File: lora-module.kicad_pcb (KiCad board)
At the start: 4 copper layers, 27.3 x 24.5 mm, 37 parts, among them P1 CONN_01X07, P2 CONN_01X07, Q1 32MHz, U2 SX1276, U5 PE4259

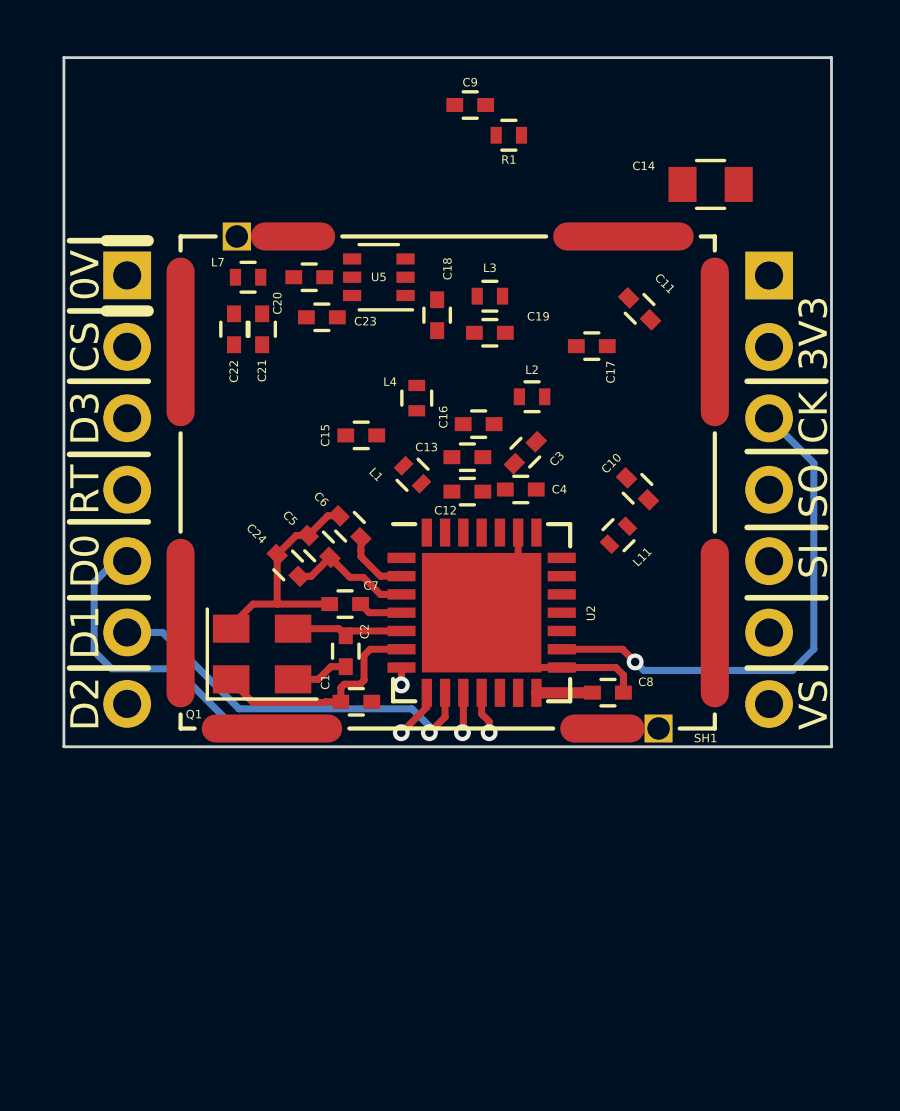
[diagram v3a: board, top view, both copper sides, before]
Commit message: added poligones for all layers
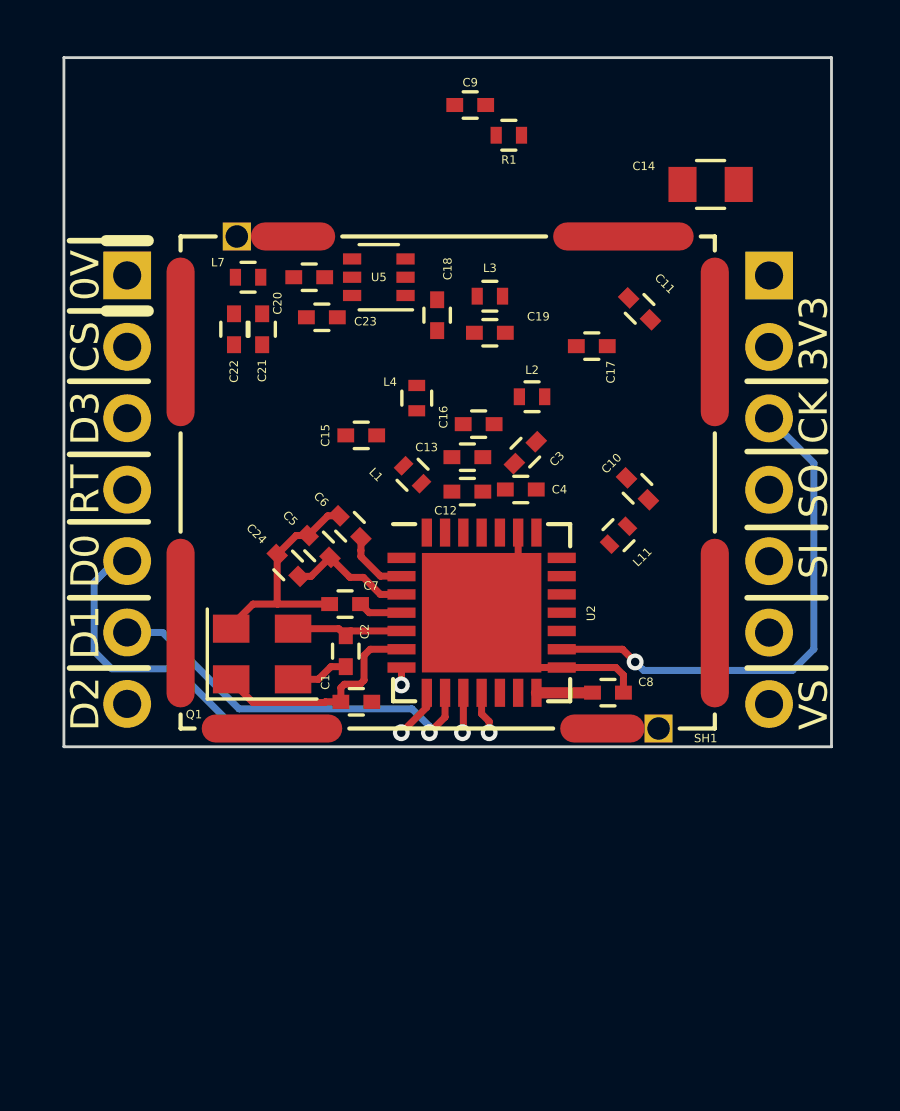
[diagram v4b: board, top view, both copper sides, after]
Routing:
- added copper zone on In2.Cu, net +3V3
- added copper zone on B.Cu, net GND
- added copper zone on F.Cu, net GND
- added copper zone on In1.Cu, net GND
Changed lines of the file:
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@@
     (links 102)
     (no_connects 67)
-    (area 84.949999 90.439999 112.57 115.42)
+    (area 84.949999 87.8 184.100001 118.35)
     (thickness 1.6)
     (drawings 65)
@@
   (segment (start 97.00625 110.88125) (end 95.19375 110.88125) (width 0.25) (layer F.Cu) (net 26))
   (segment (start 95.19375 110.88125) (end 95.025 111.05) (width 0.25) (layer F.Cu) (net 26))
+  (zone (net 2) (net_name GND) (layer In1.Cu) (hatch edge 0.508)
+    (connect_pads (clearance 0.508))
+    (min_thickness 0.254)
+    (fill yes (arc_segments 16) (thermal_gap 0.508) (thermal_bridge_width 0.508))
+    (polygon
+      (pts
+        (xy 85 115) (xy 112.3 115) (xy 112.3 90.5) (xy 85 90.5)
+      )
+    )
+  )
+  (zone (net 1) (net_name +3V3) (layer In2.Cu) (hatch edge 0.508)
+    (connect_pads (clearance 0.508))
+    (min_thickness 0.254)
+    (fill yes (arc_segments 16) (thermal_gap 0.508) (thermal_bridge_width 0.508))
+    (polygon
+      (pts
+        (xy 85 115) (xy 112.3 115) (xy 112.3 90.5) (xy 85 90.5)
+      )
+    )
+  )
+  (zone (net 2) (net_name GND) (layer B.Cu) (hatch edge 0.508)
+    (connect_pads (clearance 0.508))
+    (min_thickness 0.254)
+    (fill yes (arc_segments 16) (thermal_gap 0.508) (thermal_bridge_width 0.508))
+    (polygon
+      (pts
+        (xy 85 115) (xy 112.3 115) (xy 112.3 90.5) (xy 85 90.5)
+      )
+    )
+  )
+  (zone (net 2) (net_name GND) (layer F.Cu) (hatch edge 0.508)
+    (connect_pads (clearance 0.2))
+    (min_thickness 0.254)
+    (fill yes (arc_segments 16) (thermal_gap 0.508) (thermal_bridge_width 0.508))
+    (polygon
+      (pts
+        (xy 85 115) (xy 112.3 115) (xy 112.3 90.5) (xy 85 90.5)
+      )
+    )
+  )
 )
